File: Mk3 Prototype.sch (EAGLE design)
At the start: 192 parts, among them IC1 BD49XXX, IC2 NCP1529MU, IC3 STM32F401V, IC4 CC3100, IC5 S25FL216K0PMFI011, J1 ZX62-AB-5PA(11), J2 SFV30R-2STE1HLF, J3 SWD_SHROUD, Q1 DMMT5401, Q2 NTR4101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

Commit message: more tidying
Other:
- note added: "5x"
- note added: "Buttons"
- note added: "USB AB"
- note removed: "USB AB Socket"
- moved on the sheet: C13, C14, LED4, Q3, R18, R19, R32, R5, U1

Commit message: minor change
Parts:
- added TP7: TP4MM, TiLDA Mk3 Parts:TP4MM
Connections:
- net A5: now also TP7.TP
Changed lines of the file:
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@@
 <part name="TP14" library="TiLDA Mk3 Parts" deviceset="TP" device="B1,27"/>
 <part name="ANT2" library="TiLDA Mk3 Parts" deviceset="CHIPANT" device=""/>
+<part name="TP7" library="TiLDA Mk3 Parts" deviceset="TP" device="4MM"/>
 </parts>
 <sheets>
@@
 </instance>
 <instance part="ANT2" gate="G$1" x="736.6" y="243.84"/>
+<instance part="TP7" gate="G$1" x="617.22" y="134.62" smashed="yes" rot="R180"/>
 </instances>
 <busses>
@@
 <wire x1="617.22" y1="137.16" x2="617.22" y2="147.32" width="0.1524" layer="91"/>
 <label x="617.22" y="137.16" size="1.778" layer="95" rot="R90"/>
+<pinref part="TP7" gate="G$1" pin="TP"/>
 </segment>
 </net>

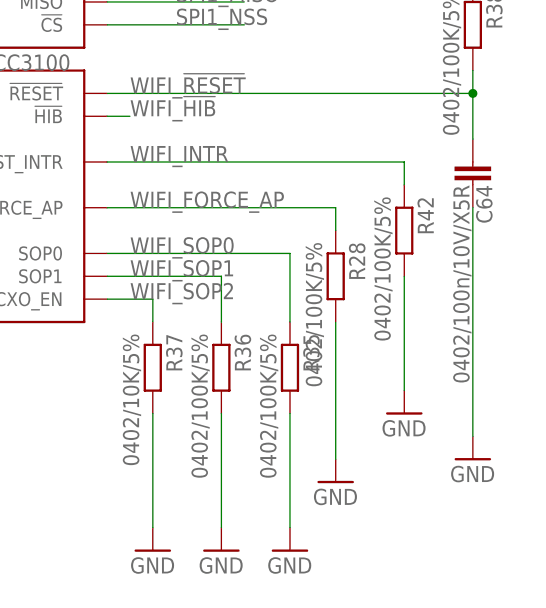
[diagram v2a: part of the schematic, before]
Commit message: Removed errant R42 resisitor and old antenna footprint
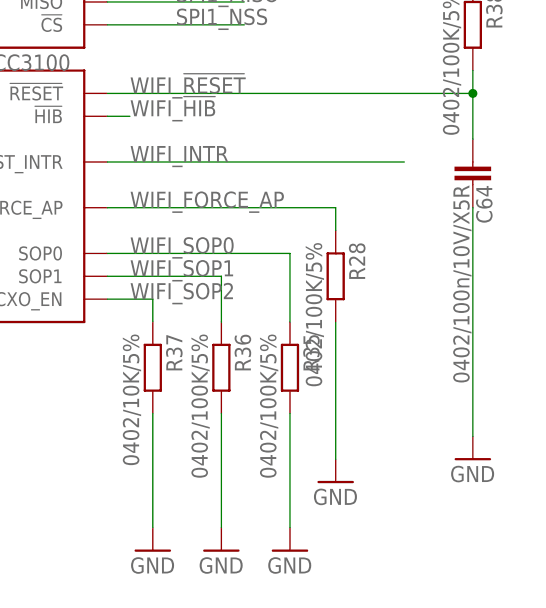
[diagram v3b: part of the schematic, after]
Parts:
- removed R42: 0402/100K/5%, TiLDA Mk3 Parts:R-EU_R0402-SMALLER
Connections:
- net GND: no longer R42.2
- net WIFI_INTR: no longer R42.1
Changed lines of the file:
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@@
 <part name="R28" library="TiLDA Mk3 Parts" deviceset="R-EU_" device="R0402-SMALLER" value="0402/100K/5%"/>
 <part name="GND44" library="TiLDA Mk3 Parts" deviceset="GND" device=""/>
-<part name="R42" library="TiLDA Mk3 Parts" deviceset="R-EU_" device="R0402-SMALLER" value="0402/100K/5%"/>
-<part name="GND45" library="TiLDA Mk3 Parts" deviceset="GND" device=""/>
 <part name="J3" library="dtb" deviceset="SWD_SHROUD" device="" value="SWD_SHROUD"/>
 <part name="GND46" library="TiLDA Mk3 Parts" deviceset="GND" device=""/>
@@
 <instance part="R28" gate="G$1" x="764.54" y="58.42" rot="R270"/>
 <instance part="GND44" gate="1" x="764.54" y="35.56"/>
-<instance part="R42" gate="G$1" x="772.16" y="63.5" rot="R270"/>
-<instance part="GND45" gate="1" x="772.16" y="43.18"/>
 <instance part="J3" gate="G$1" x="27.94" y="17.78"/>
 <instance part="GND46" gate="1" x="10.16" y="7.62"/>
@@
 </segment>
 <segment>
-<pinref part="R42" gate="G$1" pin="2"/>
-<wire x1="772.16" y1="58.42" x2="772.16" y2="45.72" width="0.1524" layer="91"/>
-<pinref part="GND45" gate="1" pin="GND"/>
-</segment>
-<segment>
 <pinref part="J3" gate="G$1" pin="GND1"/>
 <wire x1="12.7" y1="20.32" x2="10.16" y2="20.32" width="0.1524" layer="91"/>
@@
 <segment>
 <pinref part="IC4" gate="_CONTROL" pin="HOST_INTR"/>
-<pinref part="R42" gate="G$1" pin="1"/>
-<wire x1="772.16" y1="68.58" x2="772.16" y2="71.12" width="0.1524" layer="91"/>
 <wire x1="772.16" y1="71.12" x2="739.14" y2="71.12" width="0.1524" layer="91"/>
 <label x="741.68" y="71.12" size="1.778" layer="95"/>

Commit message: tweeking values of crystal caps
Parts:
- C20, C21: value 0402/6.2p/50V/NP0 -> 0402/6.0p/50V/NP0
- C65, C68: value 0402/6p2/100V/NP0 -> 0402/6.0p/50V/NP0
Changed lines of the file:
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@@
 <part name="GND18" library="TiLDA Mk3 Parts" deviceset="GND" device=""/>
 <part name="GND19" library="TiLDA Mk3 Parts" deviceset="GND" device=""/>
-<part name="C65" library="TiLDA Mk3 Parts" deviceset="C-EU" device="C0402-SMALLER" value="0402/6p2/100V/NP0"/>
-<part name="C68" library="TiLDA Mk3 Parts" deviceset="C-EU" device="C0402-SMALLER" value="0402/6p2/100V/NP0"/>
+<part name="C65" library="TiLDA Mk3 Parts" deviceset="C-EU" device="C0402-SMALLER" value="0402/6.0p/50V/NP0"/>
+<part name="C68" library="TiLDA Mk3 Parts" deviceset="C-EU" device="C0402-SMALLER" value="0402/6.0p/50V/NP0"/>
 <part name="R27" library="TiLDA Mk3 Parts" deviceset="R-EU_" device="R0402-SMALLER" value="0402/100K/5%"/>
 <part name="R34" library="TiLDA Mk3 Parts" deviceset="R-EU_" device="R0402-SMALLER" value="0402/100K/5%"/>
@@
 <part name="GND54" library="TiLDA Mk3 Parts" deviceset="GND" device=""/>
 <part name="GND55" library="TiLDA Mk3 Parts" deviceset="GND" device=""/>
-<part name="C21" library="TiLDA Mk3 Parts" deviceset="C-EU" device="C0402-SMALLER" value="0402/6.2p/50V/NP0"/>
-<part name="C20" library="TiLDA Mk3 Parts" deviceset="C-EU" device="C0402-SMALLER" value="0402/6.2p/50V/NP0"/>
+<part name="C21" library="TiLDA Mk3 Parts" deviceset="C-EU" device="C0402-SMALLER" value="0402/6.0p/50V/NP0"/>
+<part name="C20" library="TiLDA Mk3 Parts" deviceset="C-EU" device="C0402-SMALLER" value="0402/6.0p/50V/NP0"/>
 <part name="GND58" library="TiLDA Mk3 Parts" deviceset="GND" device=""/>
 <part name="R6" library="TiLDA Mk3 Parts" deviceset="R-EU_" device="R0402-SMALLER" value="0402/2k/5%"/>

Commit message: updating some part values
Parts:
- R12, R14: value (none) -> 0402/150/5%
- R2: value (none) -> 0402/220/5%
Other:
- note added: "VLS252012HBX-2R2M-1 (which is 1008 rather than 1210)"
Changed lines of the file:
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@@
 <part name="GND61" library="TiLDA Mk3 Parts" deviceset="GND" device=""/>
 <part name="LED5" library="TiLDA Mk3 Parts" deviceset="LED" device="0603-CORRECT"/>
-<part name="R2" library="TiLDA Mk3 Parts" deviceset="R-EU_" device="R0402-SMALLER"/>
+<part name="R2" library="TiLDA Mk3 Parts" deviceset="R-EU_" device="R0402-SMALLER" value="0402/220/5%"/>
 <part name="S5" library="TiLDA Mk3 Parts" deviceset="SWITCH-SPST" device="-SMD-A"/>
 <part name="+3V6" library="supply1" deviceset="+3V3" device=""/>
@@
 <part name="LED2" library="TiLDA Mk3 Parts" deviceset="LED" device="0603-CORRECT"/>
 <part name="LED3" library="TiLDA Mk3 Parts" deviceset="LED" device="0603-CORRECT"/>
-<part name="R12" library="TiLDA Mk3 Parts" deviceset="R-EU_" device="R0402-SMALLER"/>
-<part name="R14" library="TiLDA Mk3 Parts" deviceset="R-EU_" device="R0402-SMALLER"/>
+<part name="R12" library="TiLDA Mk3 Parts" deviceset="R-EU_" device="R0402-SMALLER" value="0402/150/5%"/>
+<part name="R14" library="TiLDA Mk3 Parts" deviceset="R-EU_" device="R0402-SMALLER" value="0402/150/5%"/>
 <part name="GND100" library="TiLDA Mk3 Parts" deviceset="GND" device=""/>
 <part name="GND101" library="TiLDA Mk3 Parts" deviceset="GND" device=""/>
@@
 <text x="294.64" y="144.78" size="3.81" layer="97" ratio="15">Buttons</text>
 <text x="322.834" y="160.528" size="1.778" layer="97">5x</text>
+<text x="558.8" y="127" size="1.778" layer="91">VLS252012HBX-2R2M-1 (which is 1008 rather than 1210)</text>
 </plain>
 <instances>
@@
 </segment>
 </net>
+<net name="N$36" class="0">
+<segment>
+<wire x1="558.8" y1="127" x2="584.2" y2="127" width="0.1524" layer="91"/>
+<wire x1="584.2" y1="127" x2="591.82" y2="119.38" width="0.1524" layer="91"/>
+</segment>
+</net>

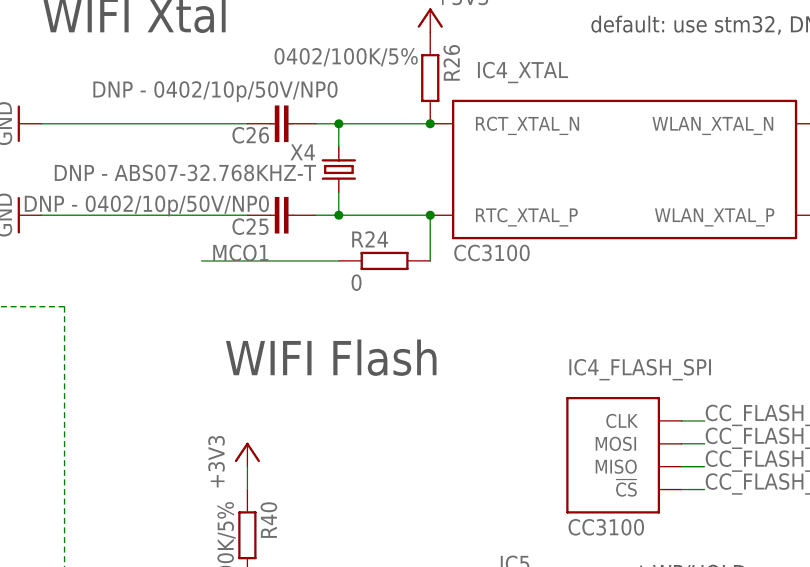
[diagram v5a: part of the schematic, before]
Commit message: one part value changed
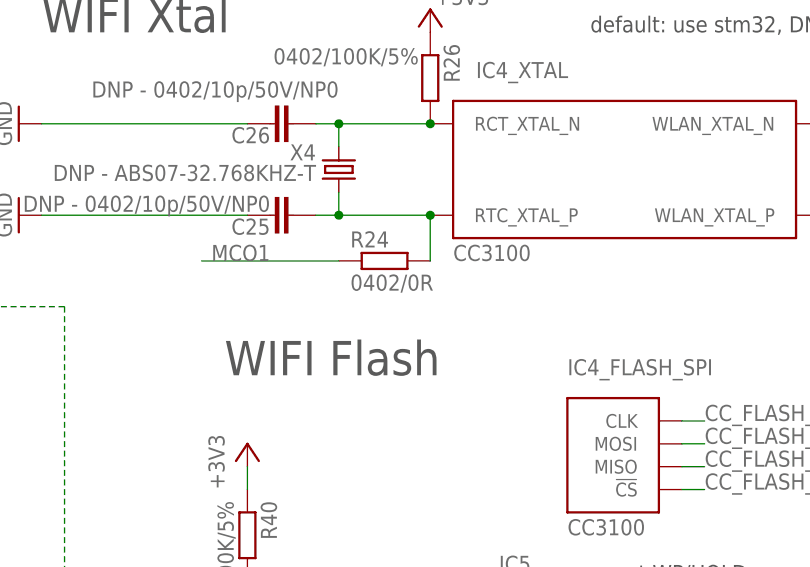
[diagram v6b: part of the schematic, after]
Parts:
- R24: value 0 -> 0402/0R
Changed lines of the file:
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@@
 <part name="R10" library="TiLDA Mk3 Parts" deviceset="R-EU_" device="R0402-SMALLER" value="0402/1k/5%"/>
 <part name="GND85" library="TiLDA Mk3 Parts" deviceset="GND" device=""/>
-<part name="R24" library="TiLDA Mk3 Parts" deviceset="R-EU_" device="R0402-SMALLER" value="0"/>
+<part name="R24" library="TiLDA Mk3 Parts" deviceset="R-EU_" device="R0402-SMALLER" value="0402/0R"/>
 <part name="SV1" library="TiLDA Mk3 Parts" deviceset="M03" device="PTH"/>
 <part name="S6" library="SparkFun-Electromechanical" deviceset="SWITCH-MOMENTARY-2" device="SMD-1101NE"/>

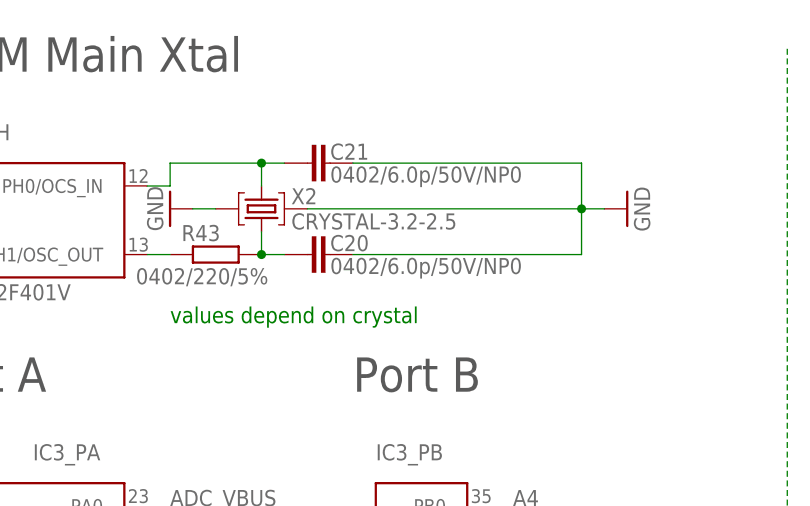
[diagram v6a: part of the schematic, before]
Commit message: added note on R45, added value to stm32 crystal
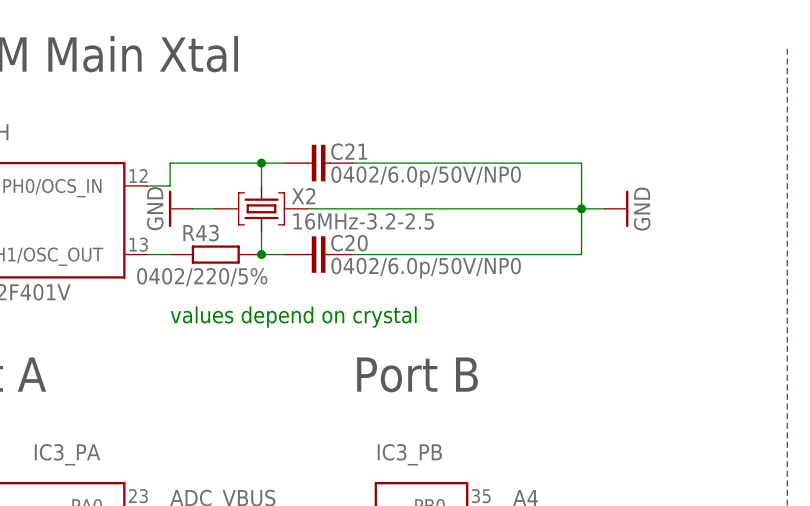
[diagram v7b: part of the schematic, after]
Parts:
- X2: value CRYSTAL-3.2-2.5 -> 16MHz-3.2-2.5
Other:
- note added: "Consider leakage here if cutoff is active and switch on"
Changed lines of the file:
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@@
 <?xml version="1.0" encoding="utf-8"?>
 <!DOCTYPE eagle SYSTEM "eagle.dtd">
-<eagle version="6.6.0">
+<eagle version="6.5.0">
 <drawing>
 <settings>
@@
 <layer number="56" name="wert" color="7" fill="1" visible="no" active="no"/>
 <layer number="57" name="tCAD" color="7" fill="1" visible="no" active="no"/>
-<layer number="90" name="Modules" color="5" fill="1" visible="no" active="yes"/>
+<layer number="90" name="Modules" color="5" fill="1" visible="yes" active="yes"/>
 <layer number="91" name="Nets" color="2" fill="1" visible="yes" active="yes"/>
 <layer number="92" name="Busses" color="1" fill="1" visible="yes" active="yes"/>
@@
 <part name="R23" library="TiLDA Mk3 Parts" deviceset="R-EU_" device="R0402-SMALLER" value="0402/22/1%"/>
 <part name="R25" library="TiLDA Mk3 Parts" deviceset="R-EU_" device="R0402-SMALLER" value="0402/22/1%"/>
-<part name="X2" library="TiLDA Mk3 Parts" deviceset="CRYSTAL" device="-3.2-2.5" value="CRYSTAL-3.2-2.5"/>
+<part name="X2" library="TiLDA Mk3 Parts" deviceset="CRYSTAL" device="-3.2-2.5" value="16MHz-3.2-2.5"/>
 <part name="GND54" library="TiLDA Mk3 Parts" deviceset="GND" device=""/>
 <part name="GND55" library="TiLDA Mk3 Parts" deviceset="GND" device=""/>
@@
 <text x="322.834" y="160.528" size="1.778" layer="97">5x</text>
 <text x="558.8" y="127" size="1.778" layer="91">VLS252012HBX-2R2M-1 (which is 1008 rather than 1210)</text>
+<text x="655.32" y="38.1" size="1.778" layer="90" rot="R270">Consider leakage here if
+cutoff is active and switch on</text>
+<wire x1="635" y1="50.8" x2="642.62" y2="50.8" width="0.1524" layer="90"/>
+<wire x1="642.62" y1="50.8" x2="655.32" y2="38.1" width="0.1524" layer="90"/>
 </plain>
 <instances>

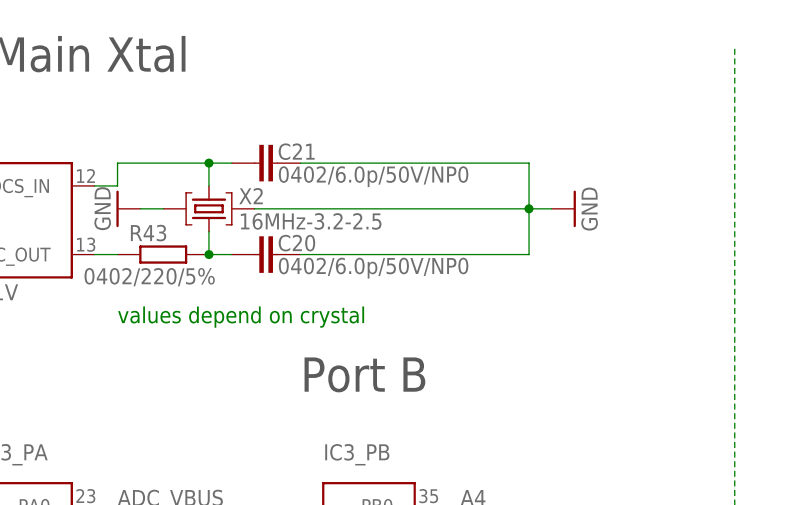
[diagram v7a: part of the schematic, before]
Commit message: updated stm32 crystal cap vales
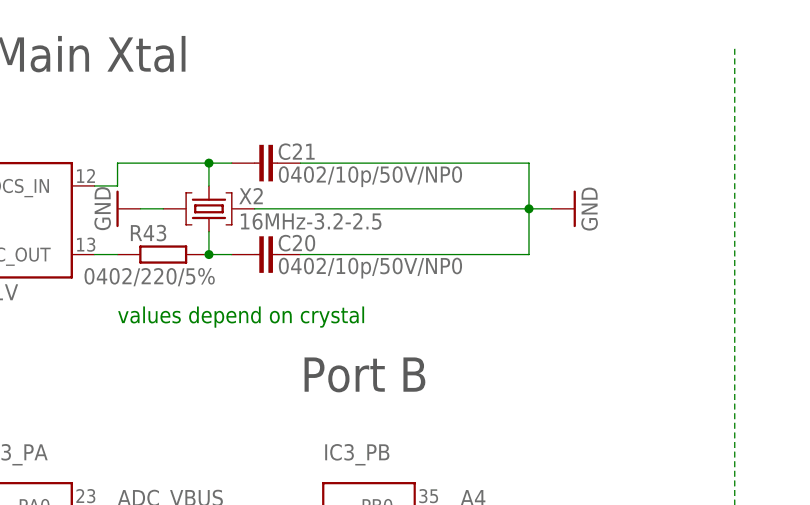
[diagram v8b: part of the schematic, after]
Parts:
- C20, C21: value 0402/6.0p/50V/NP0 -> 0402/10p/50V/NP0
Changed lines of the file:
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@@
 <part name="GND54" library="TiLDA Mk3 Parts" deviceset="GND" device=""/>
 <part name="GND55" library="TiLDA Mk3 Parts" deviceset="GND" device=""/>
-<part name="C21" library="TiLDA Mk3 Parts" deviceset="C-EU" device="C0402-SMALLER" value="0402/6.0p/50V/NP0"/>
-<part name="C20" library="TiLDA Mk3 Parts" deviceset="C-EU" device="C0402-SMALLER" value="0402/6.0p/50V/NP0"/>
+<part name="C21" library="TiLDA Mk3 Parts" deviceset="C-EU" device="C0402-SMALLER" value="0402/10p/50V/NP0"/>
+<part name="C20" library="TiLDA Mk3 Parts" deviceset="C-EU" device="C0402-SMALLER" value="0402/10p/50V/NP0"/>
 <part name="GND58" library="TiLDA Mk3 Parts" deviceset="GND" device=""/>
 <part name="R6" library="TiLDA Mk3 Parts" deviceset="R-EU_" device="R0402-SMALLER" value="0402/2k/5%"/>
